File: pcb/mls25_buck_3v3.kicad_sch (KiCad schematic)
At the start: 14 parts, among them U3 LMR51606XDBVR

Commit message: Rename `mls12` to `mls25`
Module output was changed from 12W to 25W during the course of development.
Update filenames to reflect that.
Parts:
- U3: footprint mls12:LMR51606_SOT-23-6 -> mls25:LMR51606_SOT-23-6; symbol mls12:LMR51606 -> mls25:LMR51606
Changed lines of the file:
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@@
 		)
 		(instances
-			(project "mls12"
+			(project "mls25"
 				(path "/53bda2f8-fdf0-44f4-aced-3b46017d299c/ae2a8922-e11f-4852-8a4e-ca9ff17bae0c"
 					(reference "R16")
@@
 	)
 	(symbol
-		(lib_id "mls12:LMR51606")
+		(lib_id "mls25:LMR51606")
 		(at 134.62 91.44 0)
 		(unit 1)
@@
 			)
 		)
-		(property "Footprint" "mls12:LMR51606_SOT-23-6"
+		(property "Footprint" "mls25:LMR51606_SOT-23-6"
 			(at 135.89 100.33 0)
 			(effects
@@
 		)
 		(instances
-			(project "mls12"
+			(project "mls25"
 				(path "/53bda2f8-fdf0-44f4-aced-3b46017d299c/ae2a8922-e11f-4852-8a4e-ca9ff17bae0c"
 					(reference "#PWR027")
@@
 		)
 		(instances
-			(project "mls12"
+			(project "mls25"
 				(path "/53bda2f8-fdf0-44f4-aced-3b46017d299c/ae2a8922-e11f-4852-8a4e-ca9ff17bae0c"
 					(reference "#PWR033")
@@
 		)
 		(instances
-			(project "mls12"
+			(project "mls25"
 				(path "/53bda2f8-fdf0-44f4-aced-3b46017d299c/ae2a8922-e11f-4852-8a4e-ca9ff17bae0c"
 					(reference "#PWR028")
@@
 		)
 		(instances
-			(project "mls12"
+			(project "mls25"
 				(path "/53bda2f8-fdf0-44f4-aced-3b46017d299c/ae2a8922-e11f-4852-8a4e-ca9ff17bae0c"
 					(reference "#PWR077")
@@
 		)
 		(instances
-			(project "mls12"
+			(project "mls25"
 				(path "/53bda2f8-fdf0-44f4-aced-3b46017d299c/ae2a8922-e11f-4852-8a4e-ca9ff17bae0c"
 					(reference "TP2")
@@
 		)
 		(instances
-			(project "mls12"
+			(project "mls25"
 				(path "/53bda2f8-fdf0-44f4-aced-3b46017d299c/ae2a8922-e11f-4852-8a4e-ca9ff17bae0c"
 					(reference "#PWR035")
@@
 		)
 		(instances
-			(project "mls12"
+			(project "mls25"
 				(path "/53bda2f8-fdf0-44f4-aced-3b46017d299c/ae2a8922-e11f-4852-8a4e-ca9ff17bae0c"
 					(reference "#PWR036")
@@
 		)
 		(instances
-			(project "mls12"
+			(project "mls25"
 				(path "/53bda2f8-fdf0-44f4-aced-3b46017d299c/ae2a8922-e11f-4852-8a4e-ca9ff17bae0c"
 					(reference "#PWR029")
@@
 		)
 		(instances
-			(project "mls12"
+			(project "mls25"
 				(path "/53bda2f8-fdf0-44f4-aced-3b46017d299c/ae2a8922-e11f-4852-8a4e-ca9ff17bae0c"
 					(reference "#PWR032")
@@
 		)
 		(instances
-			(project "mls12"
+			(project "mls25"
 				(path "/53bda2f8-fdf0-44f4-aced-3b46017d299c/ae2a8922-e11f-4852-8a4e-ca9ff17bae0c"
 					(reference "C22")
@@
 		)
 		(instances
-			(project "mls12"
+			(project "mls25"
 				(path "/53bda2f8-fdf0-44f4-aced-3b46017d299c/ae2a8922-e11f-4852-8a4e-ca9ff17bae0c"
 					(reference "#PWR031")
@@
 		)
 		(instances
-			(project "mls12"
+			(project "mls25"
 				(path "/53bda2f8-fdf0-44f4-aced-3b46017d299c/ae2a8922-e11f-4852-8a4e-ca9ff17bae0c"
 					(reference "C20")
@@
 		)
 		(instances
-			(project "mls12"
+			(project "mls25"
 				(path "/53bda2f8-fdf0-44f4-aced-3b46017d299c/ae2a8922-e11f-4852-8a4e-ca9ff17bae0c"
 					(reference "#PWR030")
@@
 		)
 		(instances
-			(project "mls12"
+			(project "mls25"
 				(path "/53bda2f8-fdf0-44f4-aced-3b46017d299c/ae2a8922-e11f-4852-8a4e-ca9ff17bae0c"
 					(reference "C24")
@@
 		)
 		(instances
-			(project "mls12"
+			(project "mls25"
 				(path "/53bda2f8-fdf0-44f4-aced-3b46017d299c/ae2a8922-e11f-4852-8a4e-ca9ff17bae0c"
 					(reference "C23")
@@
 		)
 		(instances
-			(project "mls12"
+			(project "mls25"
 				(path "/53bda2f8-fdf0-44f4-aced-3b46017d299c/ae2a8922-e11f-4852-8a4e-ca9ff17bae0c"
 					(reference "TP3")
@@
 		)
 		(instances
-			(project "mls12"
+			(project "mls25"
 				(path "/53bda2f8-fdf0-44f4-aced-3b46017d299c/ae2a8922-e11f-4852-8a4e-ca9ff17bae0c"
 					(reference "#PWR034")
@@
 		)
 		(instances
-			(project "mls12"
+			(project "mls25"
 				(path "/53bda2f8-fdf0-44f4-aced-3b46017d299c/ae2a8922-e11f-4852-8a4e-ca9ff17bae0c"
 					(reference "C21")
@@
 		)
 		(instances
-			(project "mls12"
+			(project "mls25"
 				(path "/53bda2f8-fdf0-44f4-aced-3b46017d299c/ae2a8922-e11f-4852-8a4e-ca9ff17bae0c"
 					(reference "R18")

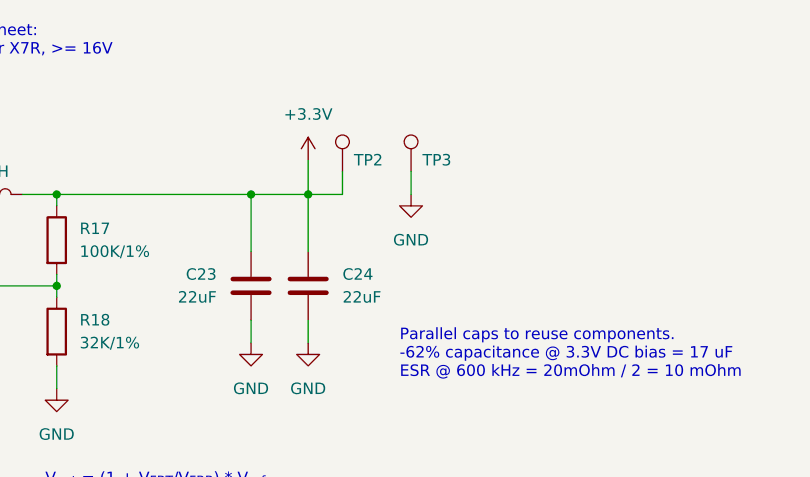
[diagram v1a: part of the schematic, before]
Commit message: Fix ERC warnings/errors
*  Add NC-flags to microcontroller pins.
*  Fix STM32 VCAP, ~RESET pin type.
*  Add PWR_FLAG symbols.
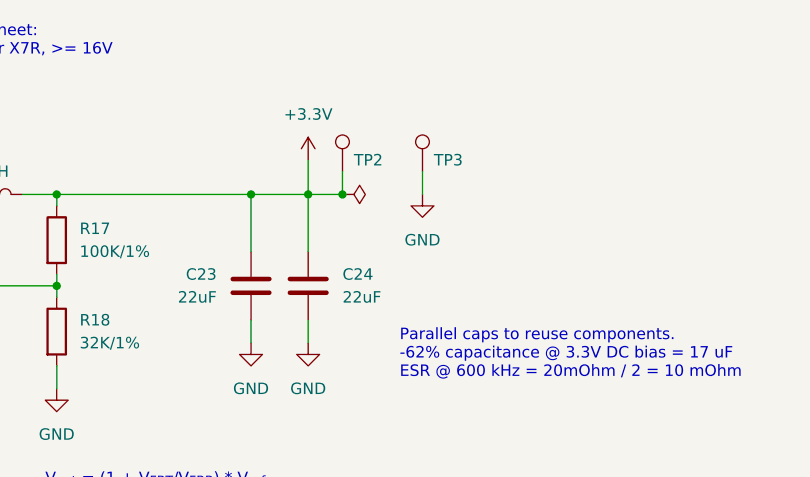
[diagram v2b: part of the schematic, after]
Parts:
- U3: MPN LMR51606XDBVR -> LMR51606
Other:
- moved on the sheet: TP3
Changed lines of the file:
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@@
 	(title_block
 		(title "3.3V buck-converter")
-		(date "2025-07-26")
+		(date "2025-09-27")
 		(rev "A")
 		(company "Quomodo BV")
@@
 	)
 	(junction
+		(at 196.85 91.44)
+		(diameter 0)
+		(color 0 0 0 0)
+	)
+	(junction
 		(at 165.1 91.44)
 		(diameter 0)
@@
 	(wire
 		(pts
-			(xy 204.47 88.9) (xy 204.47 91.44)
+			(xy 205.74 88.9) (xy 205.74 91.44)
 		)
 		(stroke
@@
 			)
 		)
-		(property "MPN" "LMR51606XDBVR"
+		(property "MPN" "LMR51606"
 			(at 134.62 91.44 0)
 			(effects
@@
 	)
 	(symbol
+		(lib_id "power:PWR_FLAG")
+		(at 196.85 91.44 270)
+		(unit 1)
+		(exclude_from_sim no)
+		(in_bom yes)
+		(on_board yes)
+		(dnp no)
+		(fields_autoplaced yes)
+		(property "Reference" "#FLG01"
+			(at 198.755 91.44 0)
+			(effects
+				(font
+					(size 1.27 1.27)
+				)
+				(hide yes)
+			)
+		)
+		(property "Value" "PWR_FLAG"
+			(at 200.66 91.4399 90)
+			(effects
+				(font
+					(size 1.27 1.27)
+				)
+				(justify left)
+				(hide yes)
+			)
+		)
+		(property "Footprint" ""
+			(at 196.85 91.44 0)
+			(effects
+				(font
+					(size 1.27 1.27)
+				)
+				(hide yes)
+			)
+		)
+		(property "Datasheet" "~"
+			(at 196.85 91.44 0)
+			(effects
+				(font
+					(size 1.27 1.27)
+				)
+				(hide yes)
+			)
+		)
+		(property "Description" "Special symbol for telling ERC where power comes from"
+			(at 196.85 91.44 0)
+			(effects
+				(font
+					(size 1.27 1.27)
+				)
+				(hide yes)
+			)
+		)
+		(property "MF" ""
+			(at 196.85 91.44 0)
+			(effects
+				(font
+					(size 1.27 1.27)
+				)
+				(hide yes)
+			)
+		)
+		(property "MPN" ""
+			(at 196.85 91.44 0)
+			(effects
+				(font
+					(size 1.27 1.27)
+				)
+				(hide yes)
+			)
+		)
+		(pin "1"
+		)
+		(instances
+			(project ""
+				(path "/53bda2f8-fdf0-44f4-aced-3b46017d299c/ae2a8922-e11f-4852-8a4e-ca9ff17bae0c"
+					(reference "#FLG01")
+					(unit 1)
+				)
+			)
+		)
+	)
+	(symbol
 		(lib_id "power:GND")
 		(at 71.12 104.14 0)
@@
 	(symbol
 		(lib_id "power:GND")
-		(at 204.47 91.44 0)
+		(at 205.74 91.44 0)
 		(unit 1)
 		(exclude_from_sim no)
@@
 		(fields_autoplaced yes)
 		(property "Reference" "#PWR077"
-			(at 204.47 97.79 0)
+			(at 205.74 97.79 0)
 			(effects
 				(font
@@
 		)
 		(property "Value" "GND"
-			(at 204.47 96.52 0)
+			(at 205.74 96.52 0)
 			(effects
 				(font
@@
 		)
 		(property "Footprint" ""
-			(at 204.47 91.44 0)
+			(at 205.74 91.44 0)
 			(effects
 				(font
@@
 		)
 		(property "Datasheet" ""
-			(at 204.47 91.44 0)
+			(at 205.74 91.44 0)
 			(effects
 				(font
@@
 		)
 		(property "Description" "Power symbol creates a global label with name \"GND\" , ground"
-			(at 204.47 91.44 0)
+			(at 205.74 91.44 0)
 			(effects
 				(font
@@
 			)
 		)
+		(property "MF" ""
+			(at 193.04 87.63 0)
+			(effects
+				(font
+					(size 1.27 1.27)
+				)
+				(hide yes)
+			)
+		)
+		(property "MPN" ""
+			(at 193.04 87.63 0)
+			(effects
+				(font
+					(size 1.27 1.27)
+				)
+				(hide yes)
+			)
+		)
 		(pin "1"
 		)
@@
 	(symbol
 		(lib_id "Connector:TestPoint")
-		(at 204.47 88.9 0)
+		(at 205.74 88.9 0)
 		(unit 1)
 		(exclude_from_sim no)
@@
 		(dnp no)
 		(property "Reference" "TP3"
-			(at 205.74 87.63 0)
+			(at 207.01 87.63 0)
 			(effects
 				(font
@@
 		)
 		(property "Value" "TestPoint"
-			(at 207.01 86.8679 0)
+			(at 208.28 86.8679 0)
 			(effects
 				(font
@@
 		)
 		(property "Footprint" "TestPoint:TestPoint_Pad_1.5x1.5mm"
-			(at 209.55 88.9 0)
+			(at 210.82 88.9 0)
 			(effects
 				(font
@@
 		)
 		(property "Datasheet" "~"
-			(at 209.55 88.9 0)
+			(at 210.82 88.9 0)
 			(effects
 				(font
@@
 		)
 		(property "Description" "test point"
-			(at 204.47 88.9 0)
+			(at 205.74 88.9 0)
 			(effects
 				(font
@@
 		)
 		(property "MF" ""
-			(at 204.47 88.9 0)
+			(at 205.74 88.9 0)
 			(effects
 				(font
@@
 		)
 		(property "MPN" ""
-			(at 204.47 88.9 0)
-			(effects
-				(font
+			(at 205.74 88.9 0)
+			(effects
+				(font

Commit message: Exclude test pads from BOM
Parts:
- TP2, TP3: now left out of the parts list
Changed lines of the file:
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@@
 		(unit 1)
 		(exclude_from_sim no)
-		(in_bom yes)
+		(in_bom no)
 		(on_board yes)
 		(dnp no)
@@
 		(unit 1)
 		(exclude_from_sim no)
-		(in_bom yes)
-		(on_board yes)
-		(dnp no)
+		(in_bom no)
+		(on_board yes)
+		(dnp no)

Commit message: Add full MPN to buck converter IC
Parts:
- U3: MPN LMR51606 -> LMR51606XDBVR
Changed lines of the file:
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@@
 			)
 		)
-		(property "MPN" "LMR51606"
+		(property "MPN" "LMR51606XDBVR"
 			(at 134.62 91.44 0)
 			(effects
